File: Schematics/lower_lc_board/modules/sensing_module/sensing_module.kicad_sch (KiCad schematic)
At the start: 22 parts, among them J5 HALL, U7 ADC_ADS131M04IPWR

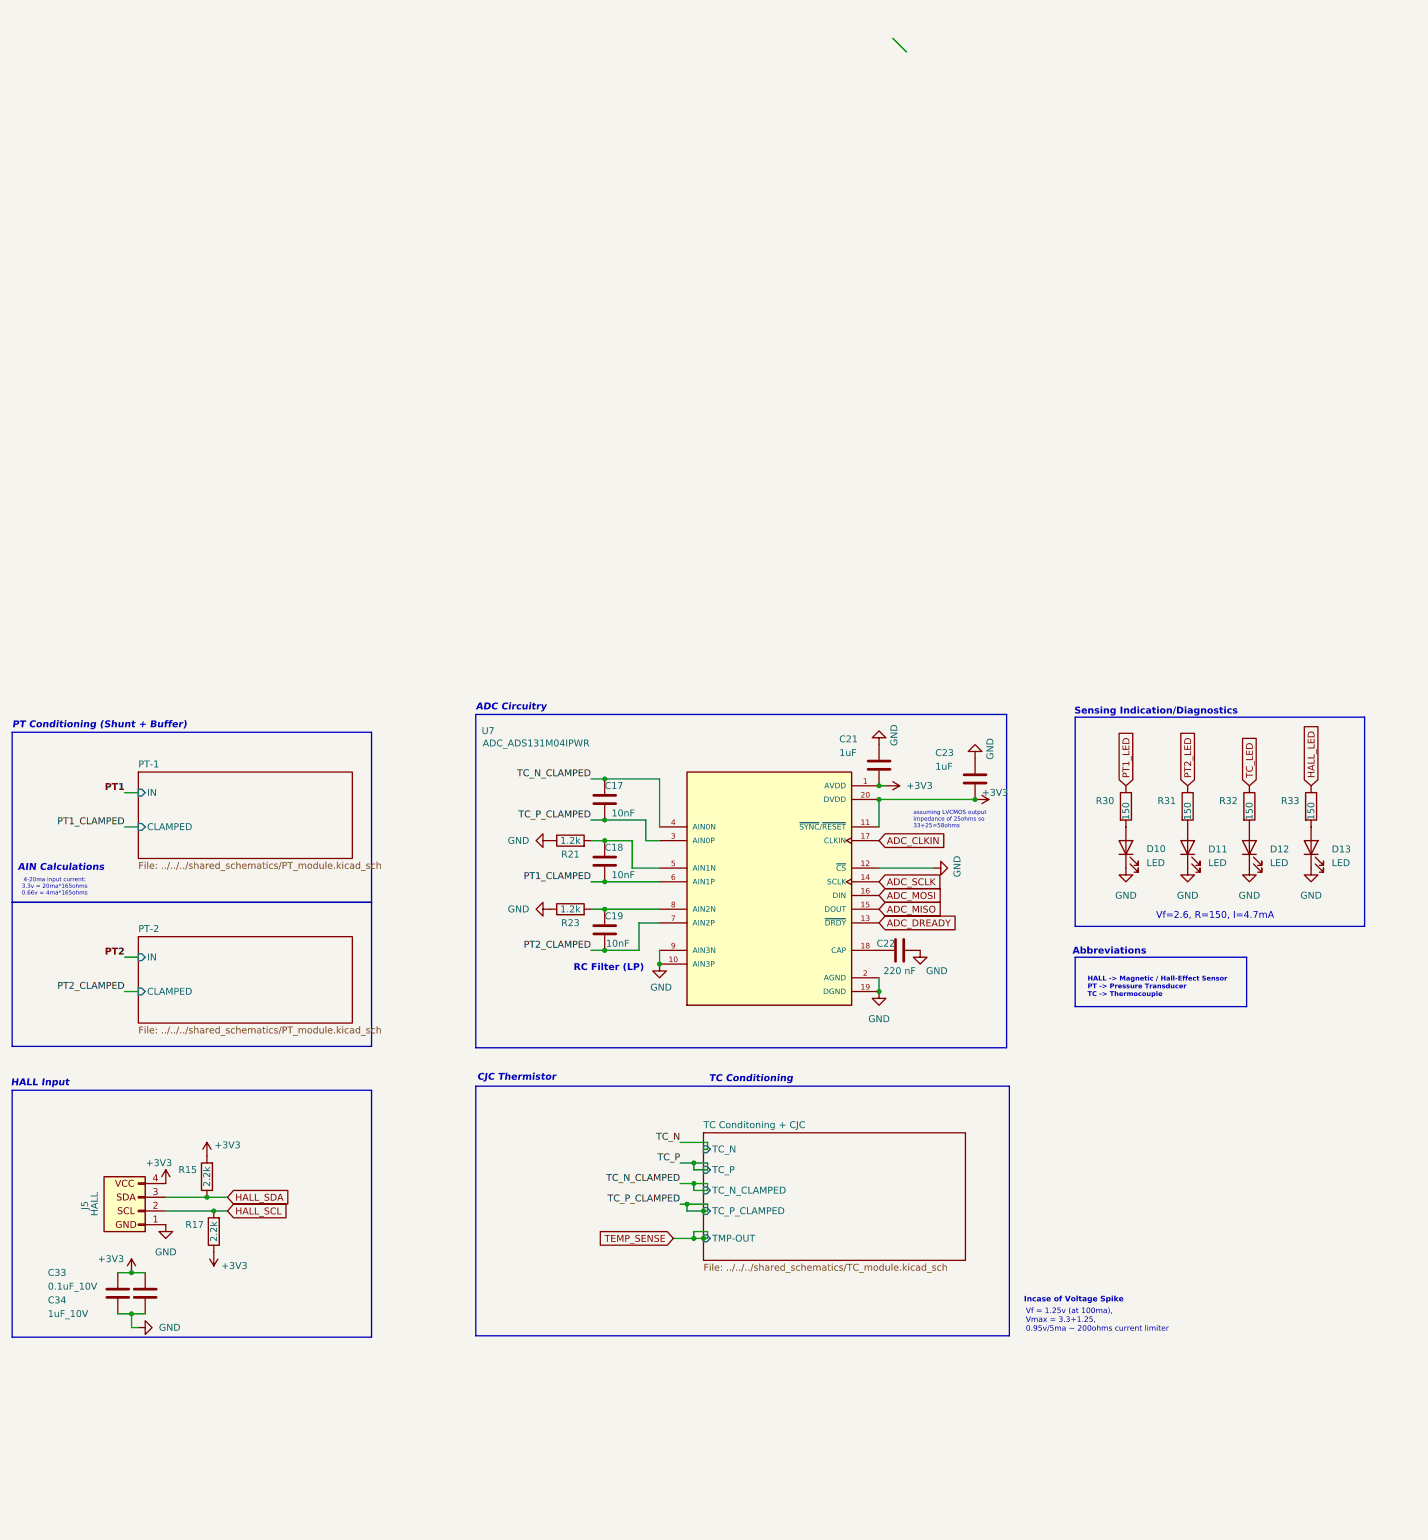
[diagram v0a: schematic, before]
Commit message: add all circuitry and missing datasheets
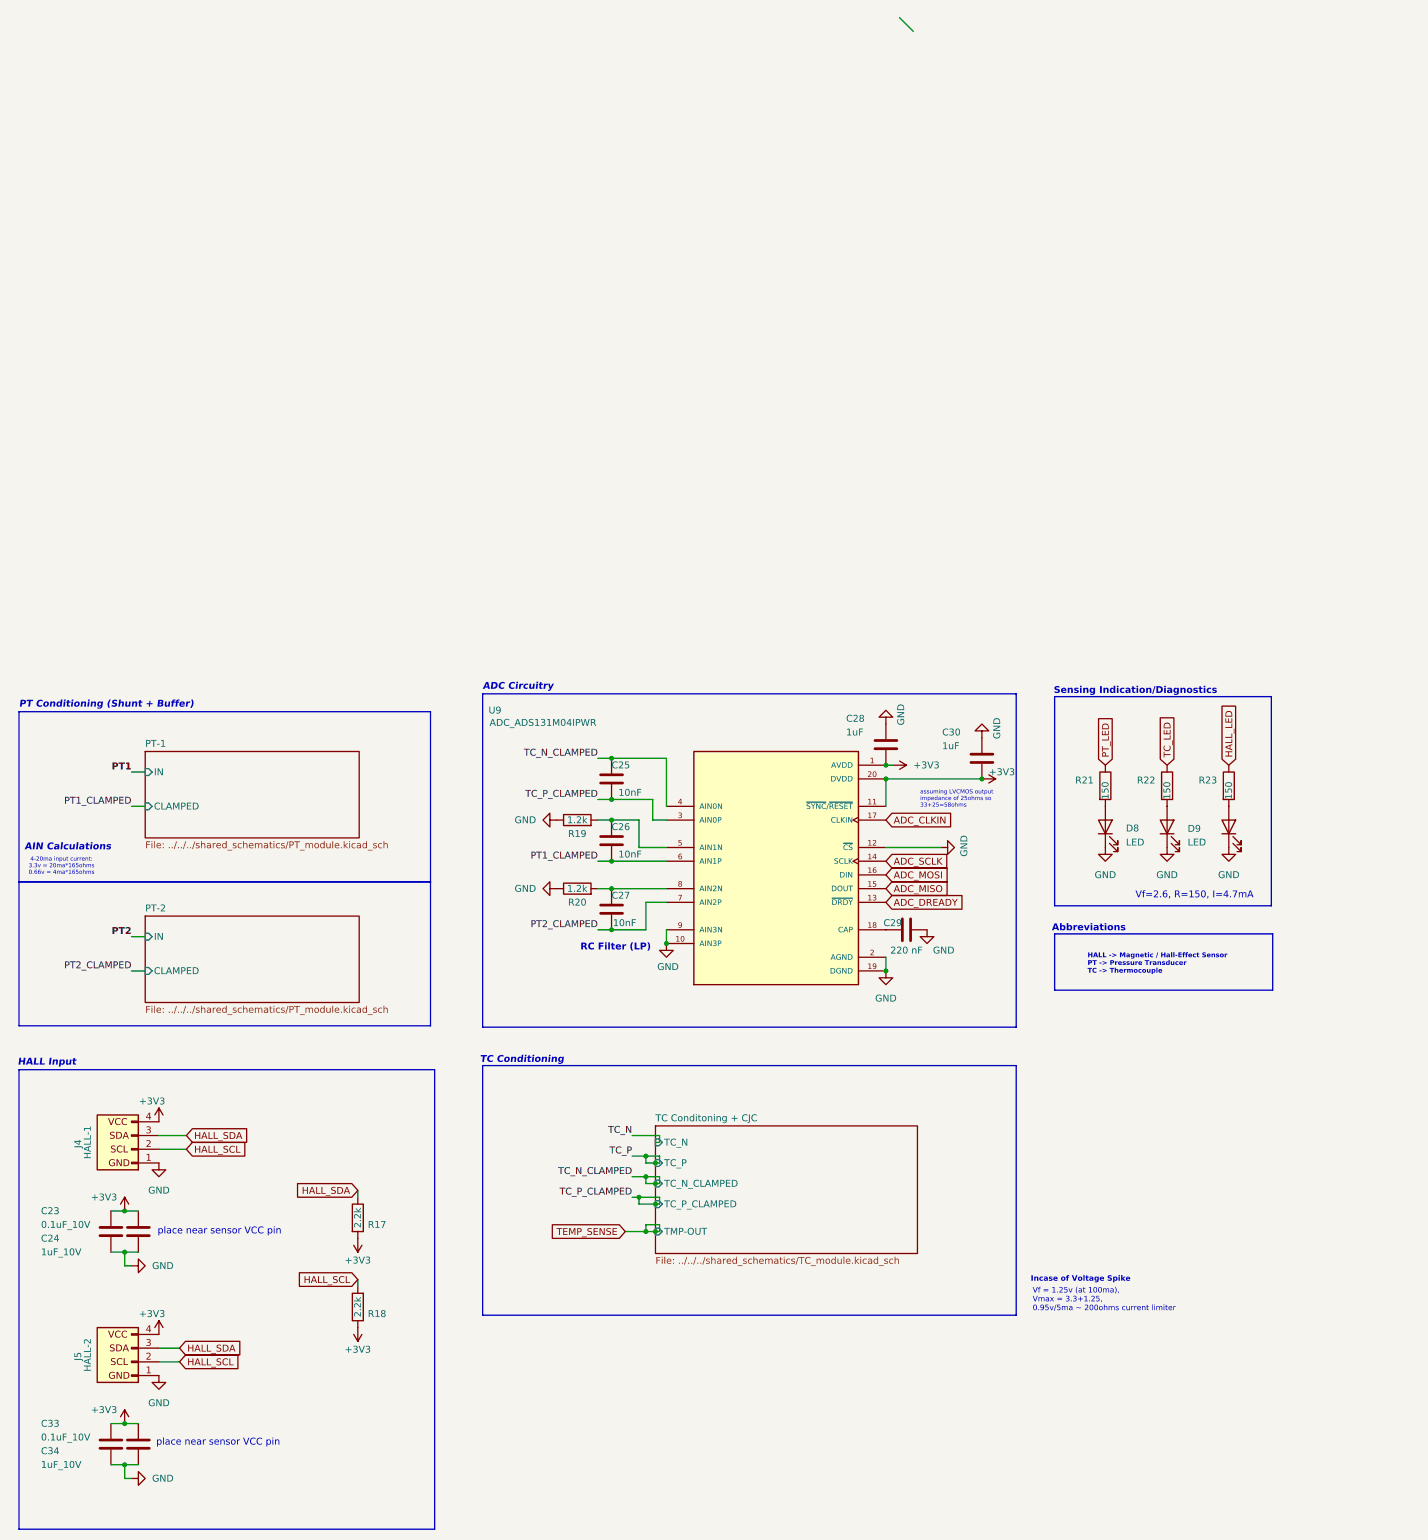
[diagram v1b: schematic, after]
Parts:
- removed C17, C18, C19: 10nF, Capacitor_SMD:C_0603_1608Metric, symbol Device:C
- removed C21: 1uF, Capacitor_SMD:C_0603_1608Metric, symbol Device:C
- removed C22: 220 nF, Capacitor_SMD:C_0805_2012Metric, symbol Device:C
- removed D11, D12, D13: LED, LED_SMD:LED_0603_1608Metric, symbol Device:LED
- removed R15: 2.2k, Resistor_SMD:R_0603_1608Metric, symbol Device:R
- removed R30, R31, R32, R33: 150, Resistor_SMD:R_0603_1608Metric, symbol Device:R
- removed U7: ADC_ADS131M04IPWR, ADS131M04IPWR:SOP65P640X120-20N, symbol ADS131M04:ADS131M04IPWR
- added C24: 1uF_10V, Capacitor_SMD:C_1206_3216Metric, symbol Device:C
- added C25, C26, C27: 10nF, Capacitor_SMD:C_0603_1608Metric, symbol Device:C
- added C28, C30: 1uF, Capacitor_SMD:C_0603_1608Metric, symbol Device:C
- added C29: 220 nF, Capacitor_SMD:C_0805_2012Metric, symbol Device:C
- added D8, D9: LED, LED_SMD:LED_0603_1608Metric, symbol Device:LED
- added J4: HALL-1, 53047-0460:MOLEX_53047-0460, symbol Connector_Generic:Conn_01x04
- added R18: 2.2k, Resistor_SMD:R_0603_1608Metric, symbol Device:R
- added R19, R20: 1.2k, Resistor_SMD:R_0603_1608Metric, symbol Device:R
- added R22: 150, Resistor_SMD:R_0603_1608Metric, symbol Device:R
- added U9: ADC_ADS131M04IPWR, ADS131M04IPWR:SOP65P640X120-20N, symbol ADS131M04:ADS131M04IPWR
- C23: value 1uF -> 0.1uF_10V; footprint Capacitor_SMD:C_0603_1608Metric -> Capacitor_SMD:C_0805_2012Metric; LCSC C15849 -> (none)
- J5: value HALL -> HALL-2
- R21, R23: value 1.2k -> 150; LCSC C22765 -> C22808
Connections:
- net +3V3: now also C23.1, R17.2, C24.1, C28.2, C30.2, J4.4 (Pin_4), R18.1, U9.1 (AVDD), U9.11 (~{SYNC}/~{RESET}), U9.20 (DVDD); no longer C23.2, R17.1
- net ADC_CLKIN: now also U9.17 (CLKIN)
- net ADC_DREADY: now also U9.13 (~{DRDY})
- net ADC_MISO: now also U9.15 (DOUT)
- net ADC_MOSI: now also U9.16 (DIN)
- net ADC_SCLK: now also U9.14 (SCLK)
- net GND: now also C23.2, C24.2, C28.1, C29.2, C30.1, D8.1 (K), D9.1 (K), J4.1 (Pin_1), R19.1, R20.1, U9.10 (AIN3P), U9.12 (~{CS}), U9.19 (DGND), U9.2 (AGND), U9.9 (AIN3N); no longer C23.1, R21.1, R23.1
- net HALL_LED: now also R23.1
- net HALL_SCL: now also J4.2 (Pin_2), R18.2; no longer R17.2
- net HALL_SDA: now also R17.1, J4.3 (Pin_3)
- net PT1_CLAMPED: now also C26.2, U9.6 (AIN1P)
- net PT2_CLAMPED: now also C27.2, U9.7 (AIN2P)
- net TC_LED: now also R22.1
- net TC_N_CLAMPED: now also C25.1, U9.4 (AIN0N)
- net TC_P_CLAMPED: now also C25.2, U9.3 (AIN0P)
- net at R23.2: now also D10.2 (A)
- net at R21.2: now also D8.2 (A)
- new net: C26.1, R19.2, U9.5 (AIN1N)
- new net: C27.1, R20.2, U9.8 (AIN2N)
- new net: D9.2 (A), R22.2
- new net: C29.1, U9.18 (CAP)
- new net PT_LED: R21.1
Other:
- note added: "place near sensor VCC pin"
- note removed: "CJC Thermistor"
- title: ULC Board Sensor Circuitry -> Lower Board Sensing Module

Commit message: pin assignments verified
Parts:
- J4, J5: footprint 53047-0460:MOLEX_53047-0460 -> S04B_PASK_2:CONN4_S04B-PASK_JST
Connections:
- net GND: no longer U9.12 (~{CS})
- net ADC_DREADY renamed ADC_DRDY
- new net ADC_CS: U9.12 (~{CS})
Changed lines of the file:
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@@
 	(wire
 		(pts
-			(xy 195.58 60.96) (xy 185.42 60.96)
-		)
-		(stroke
-			(width 0)
-			(type default)
-		)
-	)
-	(wire
-		(pts
 			(xy 139.7 60.96) (xy 144.78 60.96)
 		)
@@
 	)
 	(rectangle
-		(start 24.892 35.814)
+		(start 24.892 33.02)
 		(end 101.092 67.31)
 		(stroke
@@
 	(text "PT Conditioning (Shunt + Buffer)"
 		(exclude_from_sim no)
-		(at 24.892 34.544 0)
+		(at 24.638 31.75 0)
 		(effects
 			(font
@@
 		)
 	)
-	(global_label "ADC_DREADY"
+	(global_label "ADC_DRDY"
 		(shape input)
 		(at 185.42 71.12 0)
@@
 		)
 		(property "Intersheetrefs" "${INTERSHEET_REFS}"
-			(at 200.1376 71.12 0)
+			(at 197.9 71.12 0)
 			(effects
 				(font
@@
 		)
 	)
+	(global_label "ADC_CS"
+		(shape input)
+		(at 185.42 60.96 0)
+		(fields_autoplaced yes)
+		(effects
+			(font
+				(size 1.27 1.27)
+			)
+			(justify left)
+		)
+		(property "Intersheetrefs" "${INTERSHEET_REFS}"
+			(at 195.4809 60.96 0)
+			(effects
+				(font
+					(size 1.27 1.27)
+				)
+				(justify left)
+				(hide yes)
+			)
+		)
+	)
 	(global_label "ADC_SCLK"
 		(shape input)
@@
 	)
 	(symbol
-		(lib_id "power:GND")
-		(at 195.58 60.96 90)
-		(unit 1)
-		(exclude_from_sim no)
-		(in_bom yes)
-		(on_board yes)
-		(dnp no)
-		(property "Reference" "#PWR070"
-			(at 201.93 60.96 0)
-			(effects
-				(font
-					(size 1.27 1.27)
-				)
-				(hide yes)
-			)
-		)
-		(property "Value" "GND"
-			(at 199.898 58.674 0)
-			(effects
-				(font
-					(size 1.27 1.27)
-				)
-				(justify right)
-			)
-		)
-		(property "Footprint" ""
-			(at 195.58 60.96 0)
-			(effects
-				(font
-					(size 1.27 1.27)
-				)
-				(hide yes)
-			)
-		)
-		(property "Datasheet" "https://www.ti.com/lit/ds/symlink/drv5055.pdf?HQS=dis-dk-null-digikeymode-dsf-pf-null-wwe&ts=1641231273160"
-			(at 195.58 60.96 0)
-			(effects
-				(font
-					(size 1.27 1.27)
-				)
-				(hide yes)
-			)
-		)
-		(property "Description" "Hall effect sensor."
-			(at 195.58 60.96 0)
-			(effects
-				(font
-					(size 1.27 1.27)
-				)
-				(hide yes)
-			)
-		)
-		(pin "1"
-		)
-		(instances
-			(project "lower_lc_board"
-				(path "/d63798c4-e363-437e-9012-e4aff32e6642/c6419db7-28a9-4bfa-8244-fc88166c795c"
-					(reference "#PWR070")
-					(unit 1)
-				)
-			)
-		)
-	)
-	(symbol
 		(lib_id "power:+3V3")
 		(at 186.69 45.72 270)
@@
 			)
 		)
-		(property "Footprint" "53047-0460:MOLEX_53047-0460"
+		(property "Footprint" "S04B_PASK_2:CONN4_S04B-PASK_JST"
 			(at 45.72 156.21 0)
 			(effects
@@
 		(dnp no)
 		(property "Reference" "C29"
-			(at 186.69 74.93 90)
+			(at 193.294 74.93 90)
 			(effects
 				(font
@@
 			)
 		)
-		(property "Footprint" "53047-0460:MOLEX_53047-0460"
+		(property "Footprint" "S04B_PASK_2:CONN4_S04B-PASK_JST"
 			(at 45.72 116.84 0)
 			(effects

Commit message: replace sensing LEDs with a single
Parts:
- removed D10, D9: LED, LED_SMD:LED_0603_1608Metric, symbol Device:LED
- removed R22, R23: 150, Resistor_SMD:R_0603_1608Metric, symbol Device:R
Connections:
- net PT_LED renamed SENS_LED
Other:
- moved on the sheet: D8, R21

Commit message: finish layout
- model paths need to be fixed
- waiting for confirmation for shared folders
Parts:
- removed C24, C34: 1uF_10V, Capacitor_SMD:C_1206_3216Metric, symbol Device:C
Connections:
- net GND: no longer C28.1, C29.2, R19.1, R20.1, U9.2 (AGND)
- new net GNDA: C28.1, C29.2, R19.1, R20.1, U9.2 (AGND)
